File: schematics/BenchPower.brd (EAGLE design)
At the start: 80 x 67 mm, 24 parts, among them U1 V_REG_317SINK, U2 V_REG_317SINK, X2 9090-4R

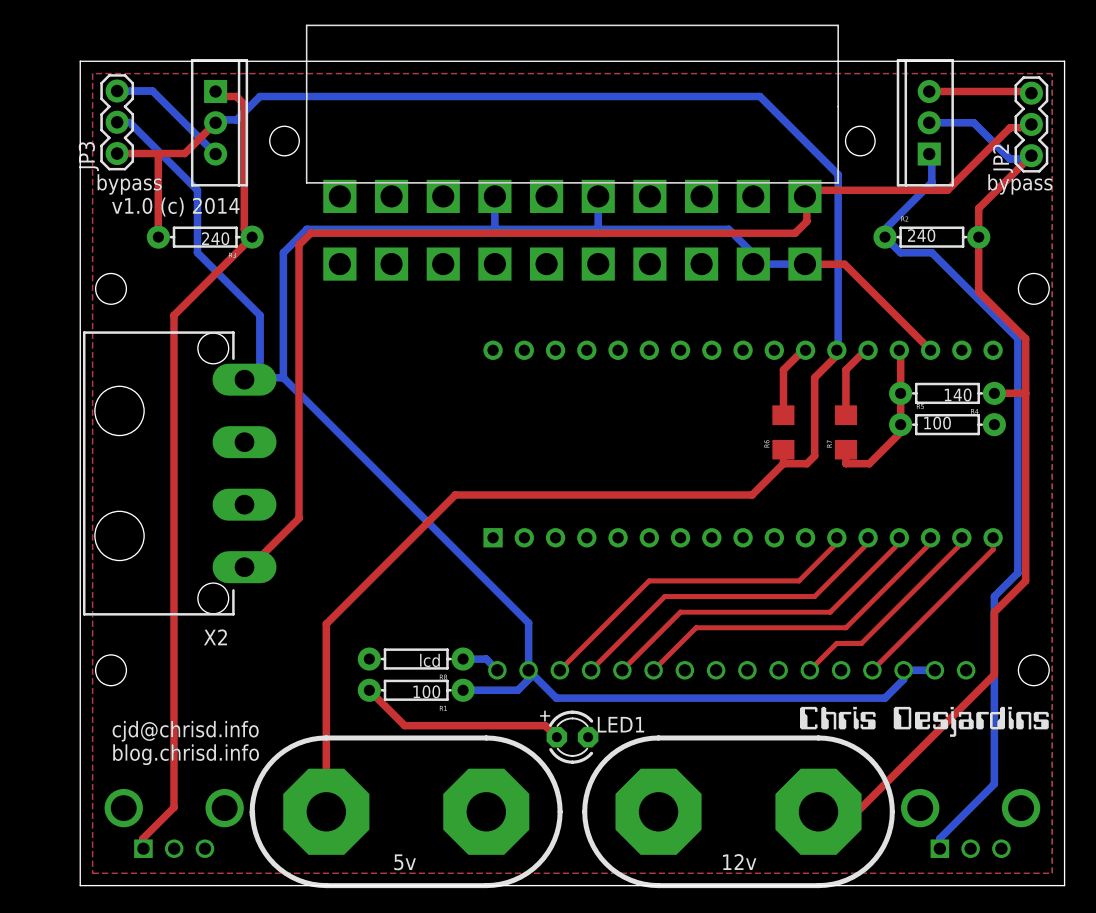
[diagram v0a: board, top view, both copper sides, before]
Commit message: Updates to bench power
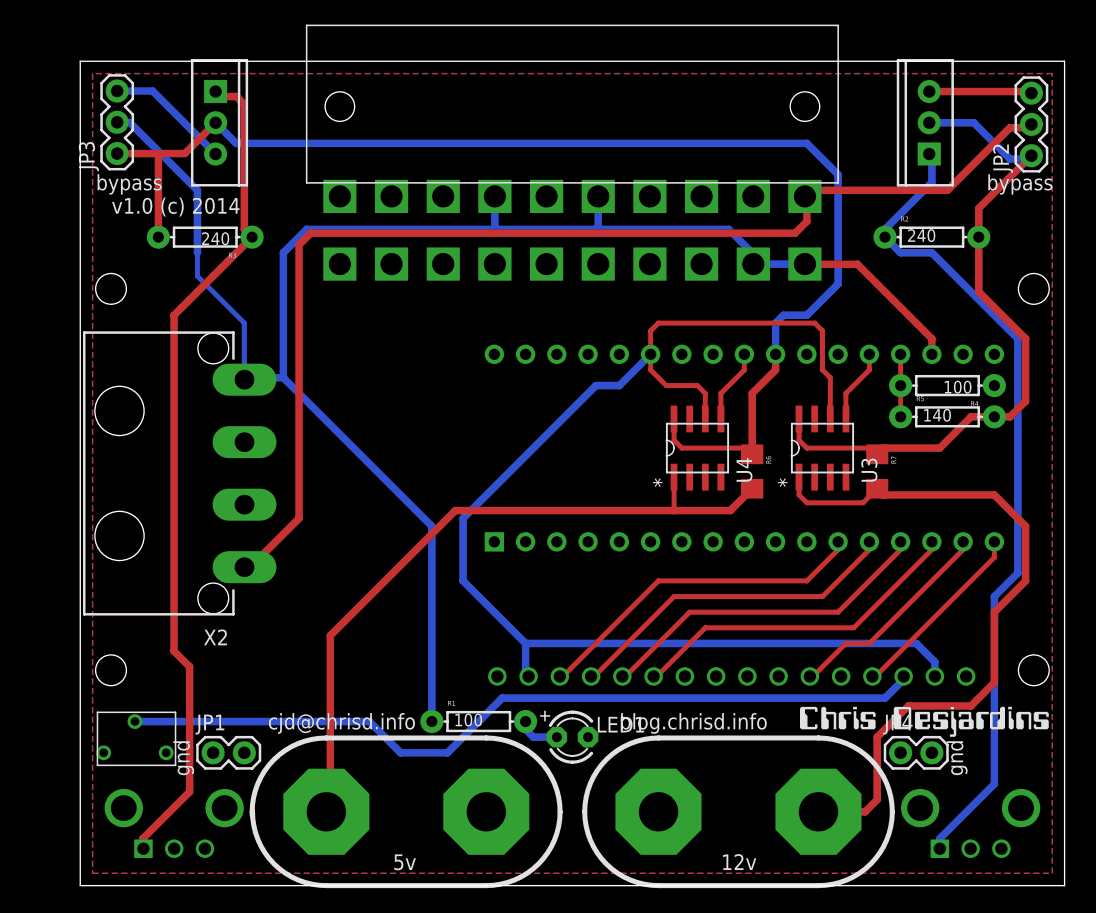
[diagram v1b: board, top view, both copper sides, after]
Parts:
- removed R8: lcd, SparkFun-Passives:AXIAL-0.3
- added JP1, JP4: M02PTH, SparkFun-Connectors:1X02
- added RV1: (no value), desjardins:3266W
- added U3, U4: AD8210YRZ, desjardins:R_8
- R4: value 140 -> 100; device SparkFun-Resistors:AXIAL-0.3 -> SparkFun-Passives:AXIAL-0.3
- R5: value 100 -> 140; device SparkFun-Resistors:AXIAL-0.3 -> SparkFun-Passives:AXIAL-0.3
- moved R1 5.68 mm to (32.4, 13.3), turned to 0 degrees
- moved R6 4.07 mm to (54.6, 33.7), turned to 270 degrees
- moved R7 4.07 mm to (64.8, 33.7), turned to 270 degrees
- moved R4 0.63 mm to (70.5, 40.6)
- moved R5 0.63 mm to (70.5, 38.1)
- moved U$2 0.35 mm to (78.1, 26.7)
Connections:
- removed net LCD_BLK: R8.P$1, U$4.P$16
- new net 12VCURRENT: U$2.P22, U3.5
- new net 5VCURRENT: U$2.P26, U4.5
- new net LCD_CONTRAST: RV1.P$2, U$4.P$3
- net 12VREG: now also R5.P$2, R7.1, U3.8; no longer PWR1.P$1, R4.P$1
- net 12VREGTAP: no longer R7.1
- net 5VARDU: now also U$4.P$15, U$4.P$2, U3.6, U4.6
- net 5VHDR: no longer U$4.P$15, U$4.P$2, U$4.P$3
- net 5VREG: now also U$2.P25, U4.8; no longer PWR2.P$1, U$2.P23
- net AMPS12VREG: now also PWR1.P$1, U3.1; no longer U$2.P22
- net AMPS5VREG: now also PWR2.P$1, U4.1; no longer U$2.P24
- net GND: now also JP1.1, JP1.2, JP4.1, JP4.2, R4.P$1, RV1.P$1, U$4.P$16, U3.2, U3.3, U3.7, U4.2, U4.3, U4.7; no longer R5.P$2, R8.P$2
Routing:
- net 5VARDU: track 0.00 -> 103.5 mm
- net LCD_CONTRAST: track 0.00 -> 66.2 mm
- net 5VREG: track 155.3 -> 103.3 mm
- net AMPS12VREG: track 6.14 -> 57.2 mm
- net AMPS5VREG: track 6.14 -> 56.4 mm
- net 5VHDR: track 176.8 -> 136.5 mm
- net 12VREG: track 77.7 -> 55.3 mm
- net N$1: track 16.8 -> 3.44 mm
- net 12VREGTAP: track 13.4 -> 5.08 mm
- net 12VCURRENT: track 0.00 -> 6.05 mm
- net 5VCURRENT: track 0.00 -> 6.05 mm
- net LCD_BLK: track 3.16 -> 0.00 mm
- net ADJREG2: track 67.2 -> 68.3 mm
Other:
- board text added: "blog.chrisd.info"
- board text added: "cjd@chrisd.info"
- board text added: "gnd"
- board text removed: "cjd@chrisd.info blog.chrisd.info"

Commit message: Use new op amp
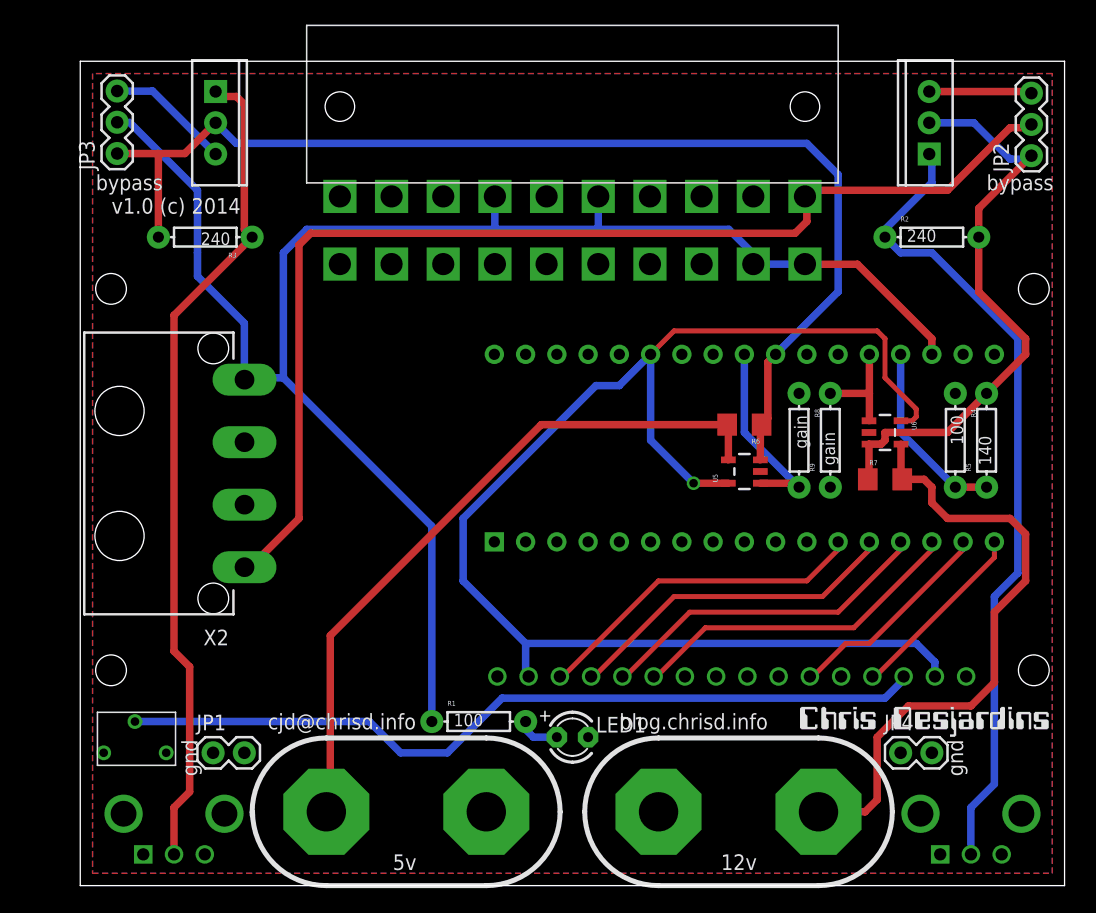
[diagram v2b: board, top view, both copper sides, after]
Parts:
- removed U3, U4: AD8210YRZ, desjardins:R_8
- added R8, R9: gain, SparkFun-Passives:AXIAL-0.3
- added U5, U6: (no value), SparkFun-AnalogIC:SOT23-5
- moved R4 4.49 mm to (71.1, 36.2), turned to 270 degrees
- moved R6 3.86 mm to (54.0, 37.5), turned to 180 degrees
- moved R5 3.70 mm to (73.7, 36.2), turned to 90 degrees
- moved R7 0.90 mm to (65.4, 33.0), turned to 0 degrees
- moved RV3 0.46 mm to (72.4, 2.54)
- moved RV4 0.46 mm to (7.62, 2.54)
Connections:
- net 12VCURRENT: now also R9.P$2, U6.1; no longer U3.5
- net 12VREG: now also U6.3; no longer U3.8
- net 5VARDU: now also U5.5, U6.5; no longer U3.6, U4.6
- net 5VCURRENT: now also R8.P$2, U5.1; no longer U4.5
- net 5VREG: now also U5.3; no longer U4.8
- net ADJREG1: now also RV3.P$2; no longer RV3.P$1
- net ADJREG2: now also RV4.P$2; no longer RV4.P$1
- net AMPS12VREG: now also U6.4; no longer U3.1
- net AMPS5VREG: now also U5.4; no longer U4.1
- net GND: now also R8.P$1, R9.P$1, U5.2, U6.2; no longer U3.2, U3.3, U3.7, U4.2, U4.3, U4.7
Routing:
- net 5VARDU: track 103.5 -> 114.5 mm, vias 0 -> 1
- net 12VREGTAP: track 5.08 -> 15.2 mm
- net 5VCURRENT: track 6.05 -> 15.9 mm
- net 5VREG: track 103.3 -> 94.0 mm
- net 12VREG: track 55.3 -> 48.2 mm
- net AMPS12VREG: track 57.2 -> 50.3 mm
- net 12VCURRENT: track 6.05 -> 8.59 mm
- net ADJREG2: track 68.3 -> 67.7 mm
- net ADJREG1: track 66.7 -> 66.1 mm

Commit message: Small routing changes
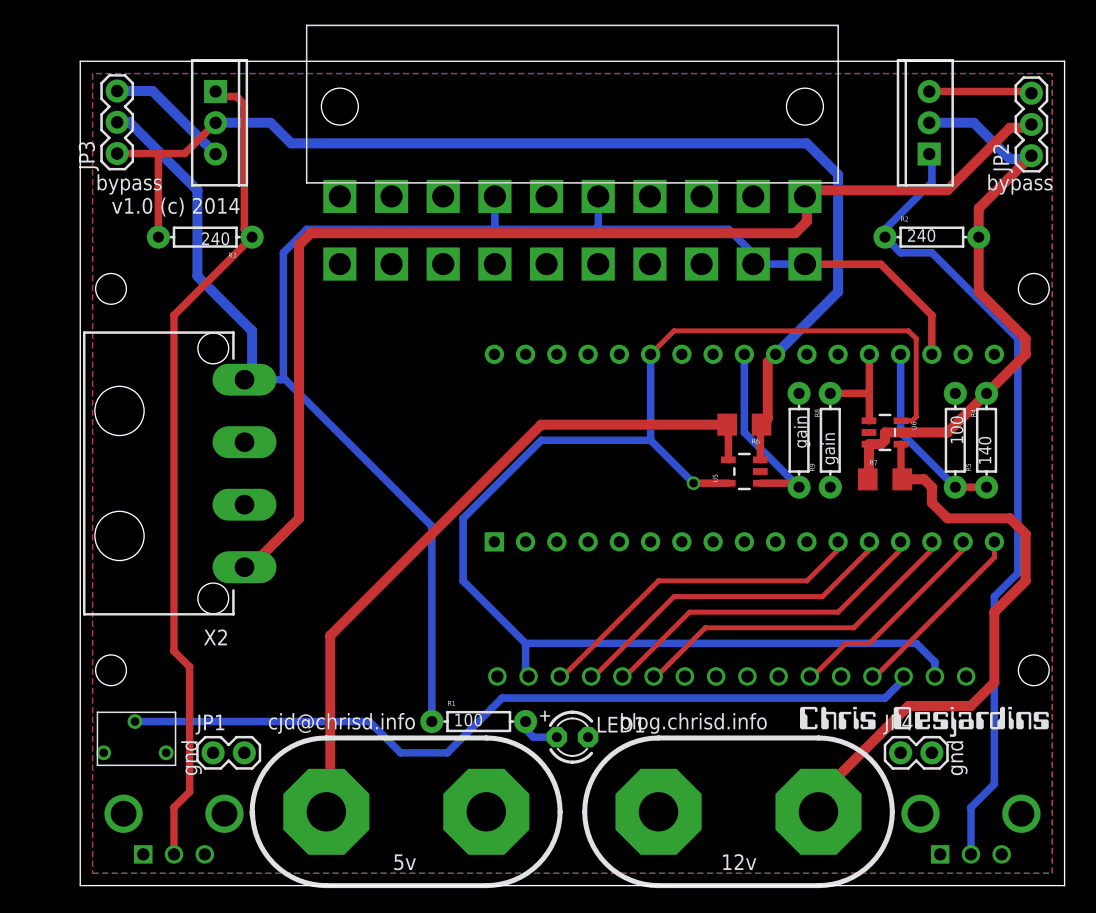
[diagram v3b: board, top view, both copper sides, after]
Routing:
- net AMPS12VREG: track 50.3 -> 48.0 mm
- net 5VHDR: track 136.5 -> 138.1 mm
- net 5VARDU: track 114.5 -> 113.1 mm

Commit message: Small routing changes
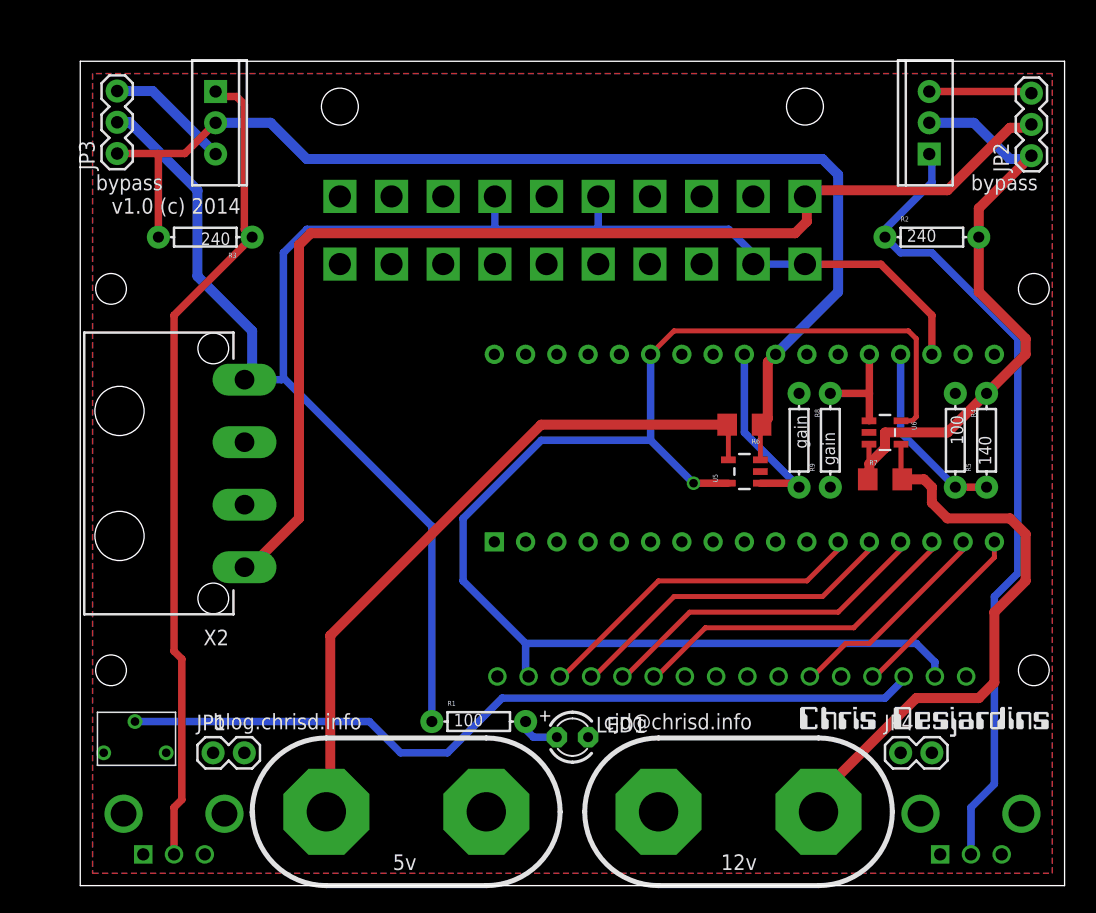
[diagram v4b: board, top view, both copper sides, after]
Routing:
- net 12VREG: track 48.2 -> 49.3 mm
- net ADJREG2: track 67.7 -> 67.1 mm
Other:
- board text removed: "gnd"
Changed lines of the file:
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@@
 <wire x1="80" y1="67" x2="0" y2="67" width="0" layer="20"/>
 <wire x1="0" y1="67" x2="0" y2="0" width="0" layer="20"/>
-<text x="15.24" y="12.7" size="1.27" layer="21">cjd@chrisd.info</text>
-<text x="2.54" y="54.61" size="1.27" layer="21">v1.0 (c) 2014</text>
-<text x="1.27" y="56.515" size="1.25" layer="21">bypass</text>
-<text x="73.66" y="56.515" size="1.25" layer="21">bypass</text>
+<text x="42.545" y="12.7" size="1.27" layer="21" font="vector">cjd@chrisd.info</text>
+<text x="2.54" y="54.61" size="1.27" layer="21" font="vector">v1.0 (c) 2014</text>
+<text x="1.27" y="56.515" size="1.25" layer="21" font="vector">bypass</text>
+<text x="72.39" y="56.515" size="1.25" layer="21" font="vector">bypass</text>
 <wire x1="13.97" y1="5.715" x2="13.97" y2="5.97" width="0.4064" layer="21"/>
 <wire x1="13.97" y1="5.97" x2="20" y2="12" width="0.4064" layer="21" curve="-90"/>
@@
 <wire x1="60" y1="0" x2="47" y2="0" width="0.4064" layer="21"/>
 <wire x1="47" y1="0" x2="41" y2="6" width="0.4064" layer="21" curve="-90"/>
-<text x="52.07" y="1.27" size="1.27" layer="21">12v</text>
-<text x="25.4" y="1.27" size="1.27" layer="21">5v</text>
-<text x="43.815" y="12.7" size="1.27" layer="21">blog.chrisd.info</text>
-<text x="9.525" y="8.89" size="1.27" layer="21" rot="R90">gnd</text>
-<text x="71.755" y="8.89" size="1.27" layer="21" rot="R90">gnd</text>
+<text x="52.07" y="1.27" size="1.27" layer="21" font="vector">12v</text>
+<text x="25.4" y="1.27" size="1.27" layer="21" font="vector">5v</text>
+<text x="10.795" y="12.7" size="1.27" layer="21" font="vector">blog.chrisd.info</text>
 </plain>
 <attributes>
@@
 <contactref element="R5" pad="P$2"/>
 <contactref element="U6" pad="3"/>
-<wire x1="64.1049" y1="35.88" x2="64.1049" y2="33.1199" width="0.8128" layer="1"/>
 <wire x1="64.1049" y1="33.1199" x2="64.005" y2="33.02" width="0.6096" layer="1"/>
-<wire x1="64.1049" y1="35.88" x2="65.09" y2="35.88" width="0.8128" layer="1"/>
-<wire x1="65.09" y1="35.88" x2="65.405" y2="36.195" width="0.8128" layer="1"/>
-<wire x1="65.405" y1="36.195" x2="65.405" y2="36.83" width="0.8128" layer="1"/>
 <wire x1="76.835" y1="44.45" x2="76.835" y2="43.18" width="0.8128" layer="1"/>
 <wire x1="76.835" y1="43.18" x2="73.66" y2="40.005" width="0.8128" layer="1"/>
 <wire x1="73.66" y1="40.005" x2="70.485" y2="36.83" width="0.8128" layer="1"/>
 <wire x1="70.485" y1="36.83" x2="65.405" y2="36.83" width="0.8128" layer="1"/>
+<wire x1="65.405" y1="36.83" x2="65.405" y2="35.56" width="0.8128" layer="1"/>
+<wire x1="65.405" y1="35.56" x2="64.135" y2="34.29" width="0.8128" layer="1"/>
+<wire x1="64.135" y1="34.29" x2="64.135" y2="33.15" width="0.8128" layer="1"/>
+<wire x1="64.135" y1="33.15" x2="64.005" y2="33.02" width="0.8128" layer="1"/>
+<wire x1="64.1049" y1="35.88" x2="64.1049" y2="34.3201" width="0.4064" layer="1"/>
+<wire x1="64.1049" y1="34.3201" x2="64.135" y2="34.29" width="0.4064" layer="1"/>
 </signal>
 <signal name="ADJREG1">
@@
 <wire x1="13.335" y1="53.34" x2="13.97" y2="52.705" width="0.6096" layer="1"/>
 <wire x1="13.97" y1="52.705" x2="7.62" y2="46.355" width="0.6096" layer="1"/>
-<wire x1="8.89" y1="7.62" x2="8.89" y2="17.78" width="0.6096" layer="1"/>
-<wire x1="8.89" y1="17.78" x2="7.62" y2="19.05" width="0.6096" layer="1"/>
+<wire x1="8.255" y1="6.985" x2="8.255" y2="18.415" width="0.6096" layer="1"/>
+<wire x1="8.255" y1="18.415" x2="7.62" y2="19.05" width="0.6096" layer="1"/>
 <wire x1="7.62" y1="19.05" x2="7.62" y2="46.355" width="0.6096" layer="1"/>
-<wire x1="8.89" y1="7.62" x2="7.62" y2="6.35" width="0.6096" layer="1"/>
+<wire x1="8.255" y1="6.985" x2="7.62" y2="6.35" width="0.6096" layer="1"/>
 <wire x1="7.62" y1="6.35" x2="7.62" y2="2.54" width="0.6096" layer="1"/>
 </signal>
@@
 <wire x1="6.35" y1="52.705" x2="6.35" y2="59.5" width="0.6096" layer="1"/>
 <contactref element="R6" pad="1"/>
-<wire x1="59.055" y1="60.325" x2="61.595" y2="57.785" width="0.8128" layer="16"/>
+<wire x1="60.325" y1="59.055" x2="61.595" y2="57.785" width="0.8128" layer="16"/>
 <contactref element="U$2" pad="P25"/>
 <wire x1="61.595" y1="57.785" x2="61.595" y2="48.26" width="0.8128" layer="16"/>
 <contactref element="U5" pad="3"/>
-<wire x1="55.2751" y1="34.605" x2="55.2751" y2="37.3651" width="0.6096" layer="1"/>
+<wire x1="55.2751" y1="34.605" x2="55.2751" y2="37.3651" width="0.4064" layer="1"/>
 <wire x1="55.2751" y1="37.3651" x2="55.375" y2="37.465" width="0.6096" layer="1"/>
 <wire x1="56.515" y1="43.18" x2="55.88" y2="42.545" width="0.8128" layer="1"/>
@@
 <wire x1="61.595" y1="48.26" x2="56.515" y2="43.18" width="0.8128" layer="16"/>
 <wire x1="11" y1="62" x2="15.47" y2="62" width="0.8128" layer="16"/>
-<wire x1="15.47" y1="62" x2="17.145" y2="60.325" width="0.8128" layer="16"/>
-<wire x1="17.145" y1="60.325" x2="59.055" y2="60.325" width="0.8128" layer="16"/>
+<wire x1="15.47" y1="62" x2="18.415" y2="59.055" width="0.8128" layer="16"/>
+<wire x1="18.415" y1="59.055" x2="60.325" y2="59.055" width="0.8128" layer="16"/>
 </signal>
 <signal name="5VARDU">
@@
 <wire x1="74.295" y1="22.225" x2="76.835" y2="24.765" width="0.8128" layer="1"/>
 <contactref element="U6" pad="4"/>
-<wire x1="66.7051" y1="35.88" x2="66.7051" y2="33.1199" width="0.6096" layer="1"/>
 <wire x1="66.7051" y1="33.1199" x2="66.805" y2="33.02" width="0.6096" layer="1"/>
 <wire x1="68.58" y1="33.02" x2="66.805" y2="33.02" width="0.8128" layer="1"/>
@@
 <wire x1="69.215" y1="31.115" x2="69.215" y2="32.385" width="0.8128" layer="1"/>
 <wire x1="69.215" y1="32.385" x2="68.58" y2="33.02" width="0.8128" layer="1"/>
-<wire x1="74.295" y1="16.51" x2="72.39" y2="14.605" width="0.8128" layer="1"/>
-<wire x1="72.39" y1="14.605" x2="67.31" y2="14.605" width="0.8128" layer="1"/>
-<wire x1="67.31" y1="14.605" x2="60.325" y2="7.62" width="0.8128" layer="1"/>
+<wire x1="74.295" y1="16.51" x2="73.025" y2="15.24" width="0.8128" layer="1"/>
+<wire x1="73.025" y1="15.24" x2="67.945" y2="15.24" width="0.8128" layer="1"/>
+<wire x1="67.945" y1="15.24" x2="60.325" y2="7.62" width="0.8128" layer="1"/>
 <wire x1="60.325" y1="7.62" x2="60.325" y2="6.325" width="0.8128" layer="1"/>
 <wire x1="60.325" y1="6.325" x2="60" y2="6" width="0.8128" layer="1"/>
+<wire x1="66.7051" y1="35.88" x2="66.7051" y2="33.1199" width="0.4064" layer="1"/>
 </signal>
 <signal name="AMPS5VREG">
@@
 <wire x1="20.32" y1="6.32" x2="20" y2="6" width="0.8128" layer="1"/>
 <contactref element="U5" pad="4"/>
-<wire x1="52.6749" y1="34.605" x2="52.6749" y2="37.3651" width="0.6096" layer="1"/>
+<wire x1="52.6749" y1="34.605" x2="52.6749" y2="37.3651" width="0.4064" layer="1"/>
 <wire x1="52.6749" y1="37.3651" x2="52.575" y2="37.465" width="0.6096" layer="1"/>
 <wire x1="37.465" y1="37.465" x2="52.575" y2="37.465" width="0.8128" layer="1"/>
